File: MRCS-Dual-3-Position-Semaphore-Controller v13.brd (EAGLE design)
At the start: 99.8 x 68.8 mm, 31 parts, among them J1 5 VDC, J2 Input, M1 SMALL_SERVO, M2 SMALL_SERVO

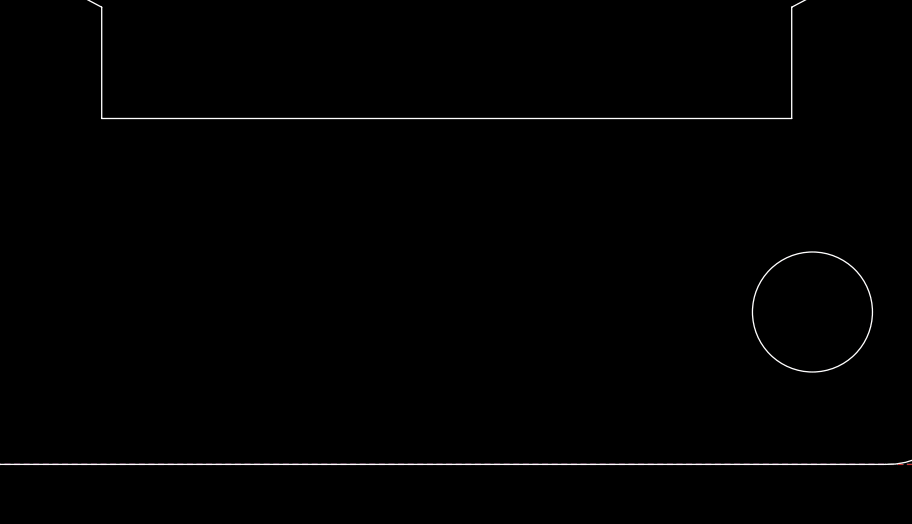
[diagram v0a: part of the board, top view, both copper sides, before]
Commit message: updates based on Holbrook's crew
added 3.5mm power terminal, added filter caps for noisy servos
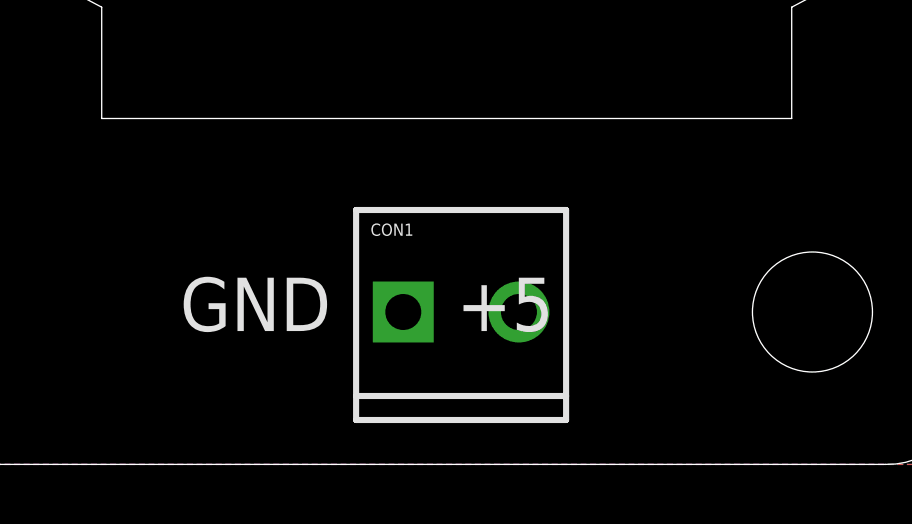
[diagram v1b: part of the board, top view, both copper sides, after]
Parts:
- added CON1: (no value), SPCoast:SCREWTERMINAL-3.5MM-2_LOCK
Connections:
- net 5V: now also CON1.2
- net GND: now also CON1.1
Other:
- board text added: "GND +5"
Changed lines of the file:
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@@
 <plain>
 <text x="20.32" y="35.56" size="1.778" layer="51" font="vector" rot="R270">USB </text>
-<text x="172.72" y="40.64" size="2.54" layer="51" font="vector" rot="R180">MRCS Dual Semaphore Controller</text>
+<text x="88.265" y="1.905" size="2.54" layer="22" font="vector" rot="MR0">MRCS Dual Semaphore Controller</text>
 <text x="73.66" y="63.5" size="1.27" layer="51" font="vector">Seth Neumann
 Earl Girbovan</text>
@@
 <text x="46.99" y="20.955" size="1.778" layer="51" font="vector" ratio="10">YEL</text>
 <text x="53.975" y="20.955" size="1.778" layer="51" font="vector" ratio="10">GRN</text>
+<text x="73.66" y="4.445" size="1.778" layer="21" font="vector" ratio="10">GND      +5</text>
 </plain>
 <attributes>
@@
 <element name="C3" library="SPCoast" package="C050-024X044" value=".01 uF" x="74.93" y="37.465" rot="R180"/>
 <element name="C4" library="SPCoast" package="E5-10.5" value="220 uF @ 35" x="6.985" y="14.605" rot="R270"/>
+<element name="CON1" library="SPCoast" package="SCREWTERMINAL-3.5MM-2_LOCK" value="" x="81.28" y="5.08"/>
 </elements>
 <signals>
@@
 <contactref element="C1" pad="2"/>
 <contactref element="C4" pad="-"/>
+<contactref element="CON1" pad="1"/>
 </signal>
 <signal name="5V" class="1">
@@
 <contactref element="C1" pad="1"/>
 <contactref element="C4" pad="+"/>
+<contactref element="CON1" pad="2"/>
 </signal>
 <signal name="A0">
